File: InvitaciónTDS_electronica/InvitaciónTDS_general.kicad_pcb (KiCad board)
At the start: 2 copper layers, 95 x 95 mm, 38 parts, among them J1 Voltage Conn, J2 FTDI Connector, Q1 2N2219, Q2 2N2219, Q3 2N2219, Q4 2N2219, Q5 2N2219, Q6 2N2219, Q7 2N2219, SW1 SW_Push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

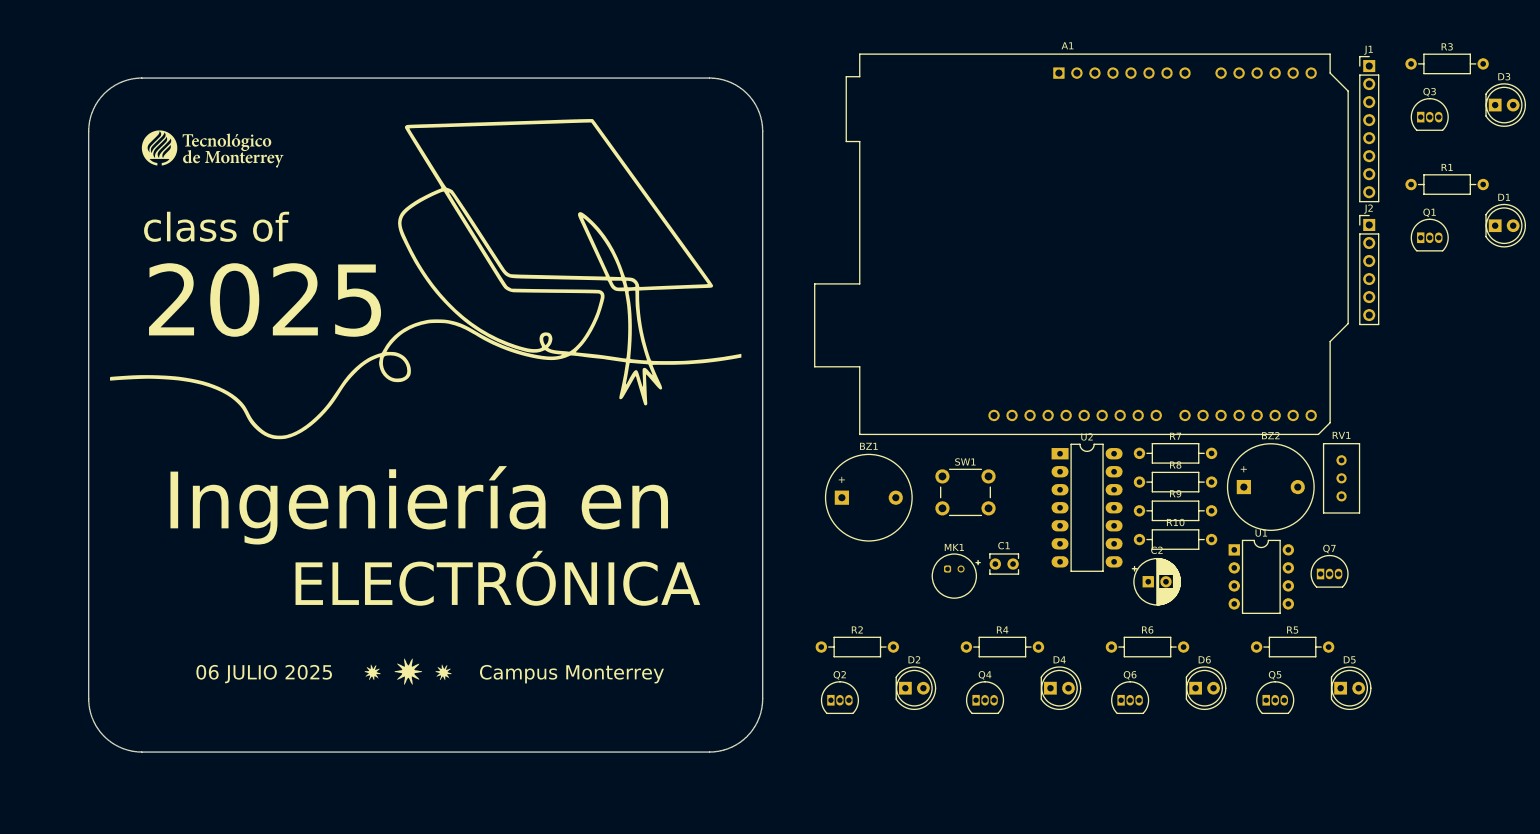
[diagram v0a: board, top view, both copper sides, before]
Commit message: Acomodo componentes Layout Electronica
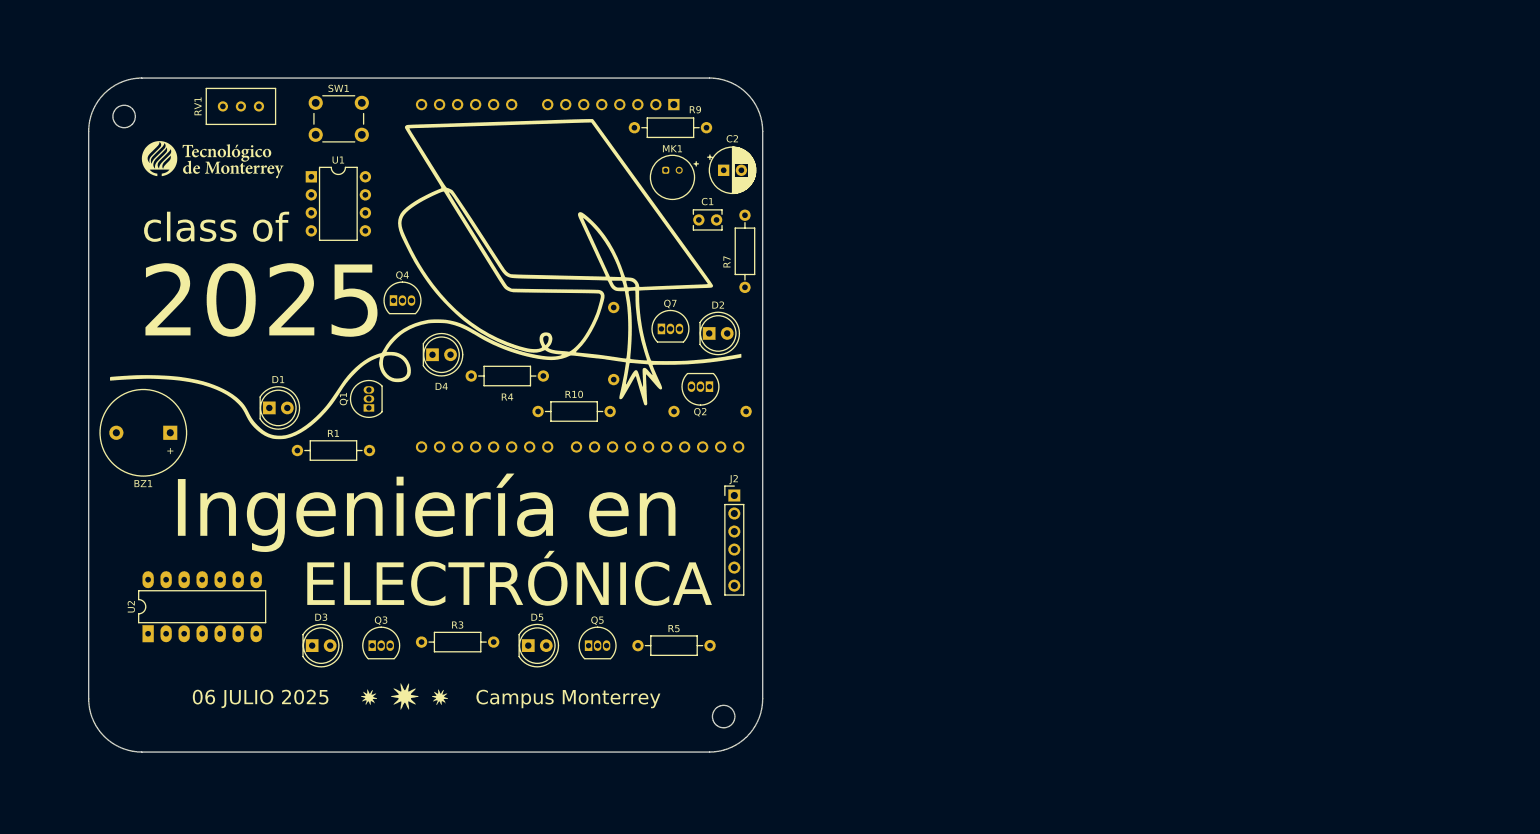
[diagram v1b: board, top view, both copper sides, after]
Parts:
- removed BZ2: Buzzer, Buzzer_Beeper:Buzzer_12x9.5RM7.6
- removed D6: LED, LED_THT:LED_D5.0mm
- removed J1: Voltage Conn, Connector_PinHeader_2.54mm:PinHeader_1x08_P2.54mm_Vertical
- removed Q6: 2N2219, Package_TO_SOT_THT:TO-92_Inline
- removed R6: R, Resistor_THT:R_Axial_DIN0207_L6.3mm_D2.5mm_P10.16mm_Horizontal
- A1, R2, R8: moved to B.Cu
- moved D3 183.3 mm to (96.5, 130.0)
- moved D1 174.7 mm to (90.5, 96.5)
- moved Q3 165.5 mm to (105.0, 130.0)
- moved RV1 165.4 mm to (83.9, 54.0), turned to 90 degrees
- moved R3 161.5 mm to (111.9, 129.5)
- moved R1 161.4 mm to (94.4, 102.5)
- moved Q1 150.2 mm to (104.5, 96.5), turned to 90 degrees
- moved U1 140.3 mm to (96.4, 63.9)
- moved U2 131.0 mm to (73.4, 128.3), turned to 90 degrees
- moved D5 114.7 mm to (127.0, 130.0)
- moved SW1 102.8 mm to (97.0, 53.5)
- moved Q4 99.6 mm to (108.0, 81.4)
- moved Q7 99.1 mm to (145.7, 85.4)
- moved D4 99.0 mm to (113.5, 89.0)
- moved J2 97.3 mm to (156.0, 108.8)
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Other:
- outline, holes or cut-outs redrawn

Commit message: PCB version 1 electronica
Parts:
- moved R2 1.16 mm to (156.5, 97.0)
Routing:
- net GND: track 0.00 -> 265.6 mm, vias 0 -> 3
- net /LEDSchem/PinName: track 0.00 -> 216.1 mm
- net Net-(A1-+5V): track 0.00 -> 135.1 mm
- net Net-(A1-D2): track 0.00 -> 74.0 mm, vias 0 -> 2
- net Net-(A1-D0/RX): track 0.00 -> 51.9 mm, vias 0 -> 1
- net Net-(A1-D6): track 0.00 -> 51.5 mm
- net Net-(A1-D1/TX): track 0.00 -> 47.7 mm, vias 0 -> 1
- net Net-(Q7-C): track 0.00 -> 45.1 mm
- net Net-(A1-A0): track 0.00 -> 39.3 mm
- net Net-(A1-A1): track 0.00 -> 37.3 mm
- net /LEDSchem2/PinName: track 0.00 -> 34.4 mm
- net Net-(Q7-B): track 0.00 -> 27.3 mm
- net Net-(Q4-B): track 0.00 -> 18.0 mm
- net Net-(MK1-+): track 0.00 -> 16.8 mm
- net Net-(D1-K): track 0.00 -> 15.1 mm
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- added copper zone on B.Cu, net GND
- added copper zone on F.Cu, net GND
